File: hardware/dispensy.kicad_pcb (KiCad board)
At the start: 2 copper layers, 125 x 100 mm, 88 parts, among them SW1 BOOTSEL, SW2 RESET, U1 DBT50G-7_62-4P, U10 RP2040, U11 SS54_C22452, U12 SS54_C22452, U13 CAN_IO, U14 TJA1042T_3_1J, U15 USB-C, U16 LM2576S-5_0_TR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

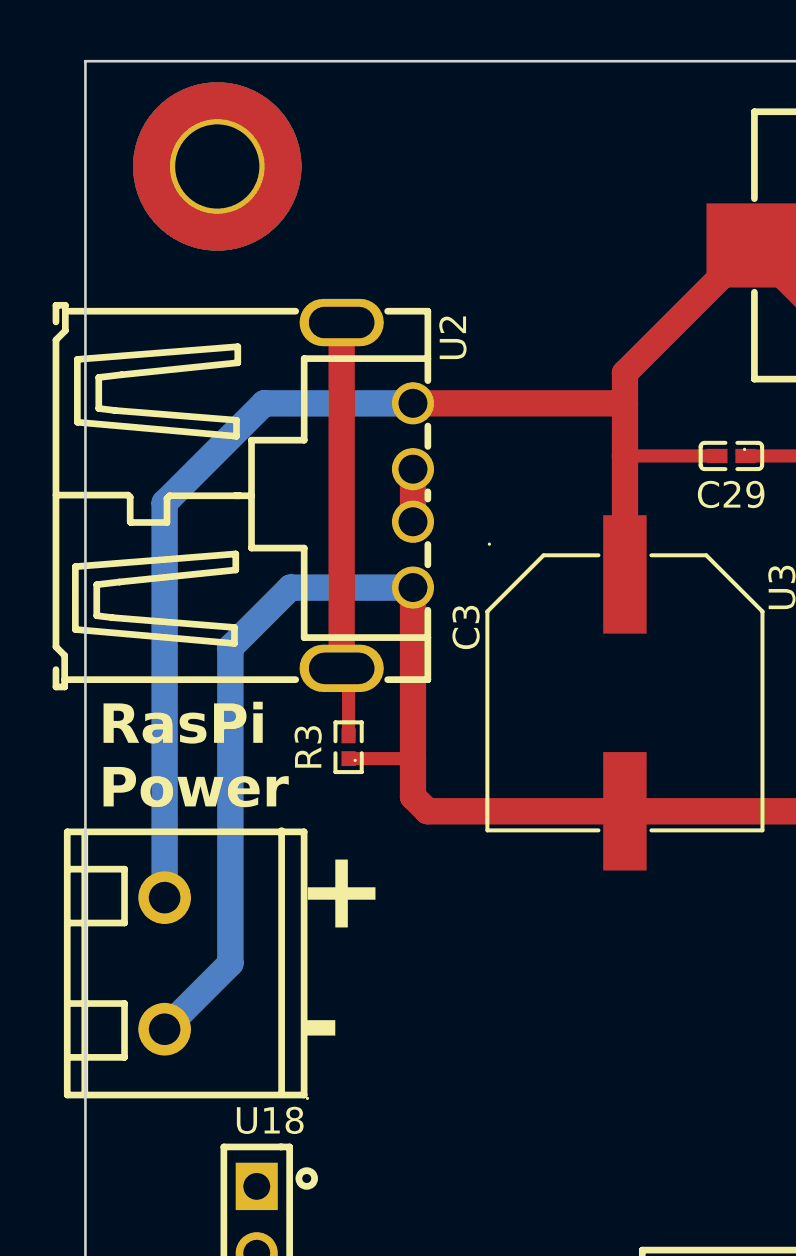
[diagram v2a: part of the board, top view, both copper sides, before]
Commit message: add resettable fuse to 5v ext output
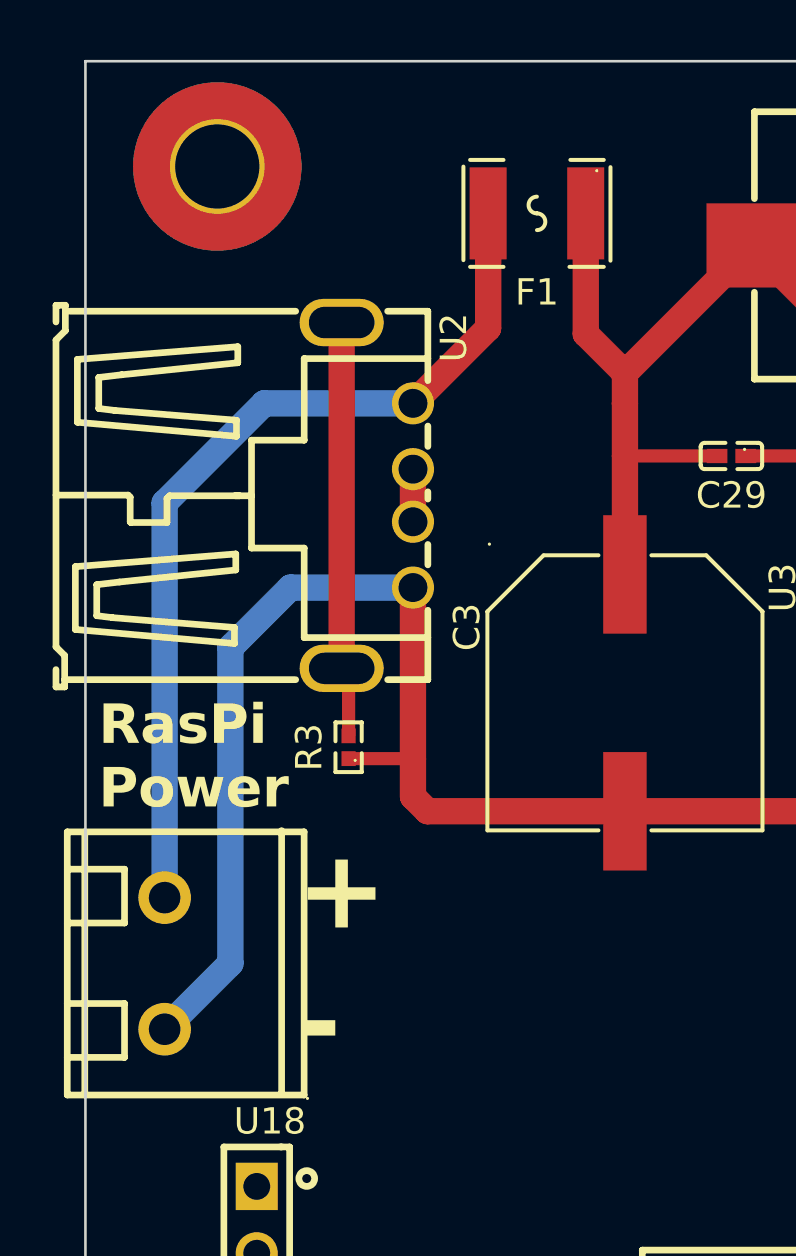
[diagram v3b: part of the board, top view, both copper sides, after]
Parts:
- added F1: ASMD1812-350-16V, jlc_footprints:F1812, F.Cu at (110.6, 53.5)
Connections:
- U18 pad 2: /EXT_PSU/Vout -> Net-(U2-VCC)
- U2 pad 1: /EXT_PSU/Vout -> Net-(U2-VCC)
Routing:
- net Net-(U2-VCC): track 0.00 -> 34.4 mm
- net /EXT_PSU/Vout: track 62.5 -> 35.1 mm
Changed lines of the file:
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@@
   (net 85 "unconnected-(U15-TX2--PadB3)")
   (net 86 "unconnected-(U15-TX2+-PadB2)")
+  (net 87 "Net-(U2-VCC)")
   (footprint "jlc_footprints:HDR-TH_3P-P2.54-V-F" (layer "F.Cu")
     (at 135.5 131.552545 180)
@@
     )
   )
+  (footprint "jlc_footprints:F1812" (layer "F.Cu")
+    (at 110.646558 53.5 180)
+    (descr "F1812 footprint")
+    (tags "F1812 footprint C2982285")
+    (property "LCSC" "C2982285")
+    (property "Sheetfile" "dispensy.kicad_sch")
+    (property "Sheetname" "")
+    (property "ki_keywords" "C2982285")
+    (attr smd)
+    (fp_text reference "F1" (at 0 -3) (layer "F.SilkS")
+        (effects (font (size 1 1) (thickness 0.15)))
+    )
+    (fp_text value "ASMD1812-350-16V" (at 0 3) (layer "F.Fab")
+        (effects (font (size 1 1) (thickness 0.15)))
+    )
+    (fp_line (start -2.794006 -1.797765) (end -2.794006 1.758242)
+      (stroke (width 0.151994) (type solid)) (layer "F.SilkS"))
+    (fp_line (start -2.540005 -2.032004) (end -1.23495 -2.032004)
+      (stroke (width 0.1524) (type solid)) (layer "F.SilkS"))
+    (fp_line (start -1.270003 2.032004) (end -2.540005 2.032004)
+      (stroke (width 0.1524) (type solid)) (layer "F.SilkS"))
+    (fp_line (start 1.270003 2.032004) (end 2.540005 2.032004)
+      (stroke (width 0.1524) (type solid)) (layer "F.SilkS"))
+    (fp_line (start 2.540005 -2.032004) (end 1.270003 -2.032004)
+      (stroke (width 0.1524) (type solid)) (layer "F.SilkS"))
+    (fp_line (start 2.794006 -1.778004) (end 2.794006 1.778004)
+      (stroke (width 0.151994) (type solid)) (layer "F.SilkS"))
+    (fp_arc (start 0 0) (mid -0.317501 -0.317501) (end 0 -0.635002)
+      (stroke (width 0.151994) (type solid)) (layer "F.SilkS"))
+    (fp_arc (start 0 0) (mid 0.317501 0.317501) (end 0 0.635002)
+      (stroke (width 0.151994) (type solid)) (layer "F.SilkS"))
+    (fp_circle (center -2.275083 1.620015) (end -2.24511 1.620015)
+      (stroke (width 0.059995) (type solid)) (fill none) (layer "F.SilkS"))
+    (pad "1" smd rect (at -1.853442 0 180) (size 1.40668 3.499213) (layers "F.Cu" "F.Paste" "F.Mask")
+      (net 4 "/EXT_PSU/Vout") (pinfunction "1") (pintype "unspecified"))
+    (pad "2" smd rect (at 1.853442 0 180) (size 1.40668 3.499213) (layers "F.Cu" "F.Paste" "F.Mask")
+      (net 87 "Net-(U2-VCC)") (pinfunction "2") (pintype "unspecified"))
+    (model "jlc_lib/jlc_footprints/packages3d/F1812.step"
+      (offset (xyz 0 0 0))
+      (scale (xyz 1 1 1))
+      (rotate (xyz 0 0 0))
+    )
+  )
   (footprint "jlc_footprints:C0402" (layer "F.Cu")
     (at 125 114.25 -90)
@@
     )
     (fp_line (start -5.000127 -3.7) (end -5.000127 5.300025)
-      (stroke (width 0.254001) (type solid)) (layer "F.SilkS"))
+      (stroke (width 0.254) (type solid)) (layer "F.SilkS"))
     (fp_line (start -5.000127 -3.7) (end 4.999873 -3.7)
-      (stroke (width 0.254001) (type solid)) (layer "F.SilkS"))
+      (stroke (width 0.254) (type solid)) (layer "F.SilkS"))
     (fp_line (start -5.000127 -3.033985) (end 4.999873 -3.033985)
-      (stroke (width 0.254001) (type solid)) (layer "F.SilkS"))
+      (stroke (width 0.254) (type solid)) (layer "F.SilkS"))
     (fp_line (start -5.000127 5.300025) (end 4.999873 5.300025)
-      (stroke (width 0.254001) (type solid)) (layer "F.SilkS"))
+      (stroke (width 0.254) (type solid)) (layer "F.SilkS"))
     (fp_line (start -4.952985 4.445034) (end 5.047015 4.445034)
-      (stroke (width 0.254001) (type solid)) (layer "F.SilkS"))
+      (stroke (width 0.254) (type solid)) (layer "F.SilkS"))
     (fp_line (start -3.569469 -3.7) (end -3.569469 -1.524003)
-      (stroke (width 0.254001) (type solid)) (layer "F.SilkS"))
+      (stroke (width 0.254) (type solid)) (layer "F.SilkS"))
     (fp_line (start -3.569469 -1.524003) (end -1.524003 -1.524003)
-      (stroke (width 0.254001) (type solid)) (layer "F.SilkS"))
+      (stroke (width 0.254) (type solid)) (layer "F.SilkS"))
     (fp_line (start -1.524003 -1.524003) (end -1.524003 -3.7)
-      (stroke (width 0.254001) (type solid)) (layer "F.SilkS"))
+      (stroke (width 0.254) (type solid)) (layer "F.SilkS"))
     (fp_line (start 1.535941 -3.7) (end 1.535941 -1.524003)
-      (stroke (width 0.254001) (type solid)) (layer "F.SilkS"))
+      (stroke (width 0.254) (type solid)) (layer "F.SilkS"))
     (fp_line (start 1.535941 -1.524003) (end 3.581407 -1.524003)
-      (stroke (width 0.254001) (type solid)) (layer "F.SilkS"))
+      (stroke (width 0.254) (type solid)) (layer "F.SilkS"))
     (fp_line (start 3.581407 -1.524003) (end 3.581407 -3.7)
-      (stroke (width 0.254001) (type solid)) (layer "F.SilkS"))
+      (stroke (width 0.254) (type solid)) (layer "F.SilkS"))
     (fp_line (start 4.999873 -3.7) (end 4.999873 5.300025)
-      (stroke (width 0.254001) (type solid)) (layer "F.SilkS"))
+      (stroke (width 0.254) (type solid)) (layer "F.SilkS"))
     (fp_circle (center -5.127127 5.426975) (end -5.097155 5.426975)
       (stroke (width 0.059995) (type solid)) (fill none) (layer "F.SilkS"))
@@
       (net 1 "GND") (pinfunction "1") (pintype "unspecified"))
     (pad "2" thru_hole circle (at 2.5 0 90) (size 2 2) (drill 1.2) (layers "*.Cu" "*.Mask")
-      (net 4 "/EXT_PSU/Vout") (pinfunction "2") (pintype "unspecified"))
+      (net 87 "Net-(U2-VCC)") (pinfunction "2") (pintype "unspecified"))
     (model "jlc_lib/jlc_footprints/packages3d/CONN-TH_XY300V-A-5.0-2P.step"
       (offset (xyz 0.2120645968 -0.799998388 6.250050906))
@@
       (stroke (width 0.4) (type solid)) (fill none) (layer "F.Fab"))
     (pad "1" thru_hole circle (at -3.499873 -1.354966 270) (size 1.6 1.6) (drill 1.100025) (layers "*.Cu" "*.Mask")
-      (net 4 "/EXT_PSU/Vout") (pinfunction "VCC") (pintype "unspecified"))
+      (net 87 "Net-(U2-VCC)") (pinfunction "VCC") (pintype "unspecified"))
     (pad "2" thru_hole circle (at -1 -1.354966 270) (size 1.6 1.6) (drill 1.100025) (layers "*.Cu" "*.Mask")
       (net 63 "Net-(U2-D+)") (pinfunction "D-") (pintype "unspecified"))
@@
   (segment (start 113.990456 62.717646) (end 113.990456 60.717646) (width 1) (layer "F.Cu") (net 4))
   (segment (start 124.290431 62.85087) (end 124.290431 60.167735) (width 1) (layer "F.Cu") (net 4))
-  (segment (start 105.936735 60.717773) (end 113.990329 60.717773) (width 1) (layer "F.Cu") (net 4))
+  (segment (start 112.5 58.077076) (end 113.990456 59.567532) (width 1) (layer "F.Cu") (net 4))
+  (segment (start 112.5 53.5) (end 112.5 58.077076) (width 1) (layer "F.Cu") (net 4))
   (segment (start 124.290431 60.167735) (end 118.840342 54.717646) (width 1) (layer "F.Cu") (net 4))
   (segment (start 113.990456 59.567532) (end 118.840342 54.717646) (width 1) (layer "F.Cu") (net 4))
@@
   (segment (start 113.990456 67.217773) (end 113.990456 62.717646) (width 1) (layer "F.Cu") (net 4))
   (segment (start 117.490456 62.717646) (end 113.990456 62.717646) (width 0.5) (layer "F.Cu") (net 4))
-  (segment (start 96.5 79.5) (end 96.5 64.5) (width 1) (layer "B.Cu") (net 4))
-  (segment (start 96.5 64.5) (end 100.282227 60.717773) (width 1) (layer "B.Cu") (net 4))
-  (segment (start 100.282227 60.717773) (end 105.936735 60.717773) (width 1) (layer "B.Cu") (net 4))
   (segment (start 191.754966 80.907765) (end 194.254966 80.907765) (width 0.5) (layer "F.Cu") (net 5))
   (segment (start 191.484963 89.177768) (end 194.984963 89.177768) (width 0.5) (layer "F.Cu") (net 5))
@@
   (segment (start 157.5 131.552545) (end 156 130.052545) (width 0.2) (layer "B.Cu") (net 76))
   (segment (start 156 130.052545) (end 155 130.052545) (width 0.2) (layer "B.Cu") (net 76))
+  (segment (start 108.793116 57.861392) (end 105.936735 60.717773) (width 1) (layer "F.Cu") (net 87))
+  (segment (start 108.793116 53.5) (end 108.793116 57.861392) (width 1) (layer "F.Cu") (net 87))
+  (segment (start 96.5 79.5) (end 96.5 64.5) (width 1) (layer "B.Cu") (net 87))
+  (segment (start 96.5 64.5) (end 100.282227 60.717773) (width 1) (layer "B.Cu") (net 87))
+  (segment (start 100.282227 60.717773) (end 105.936735 60.717773) (width 1) (layer "B.Cu") (net 87))
 )

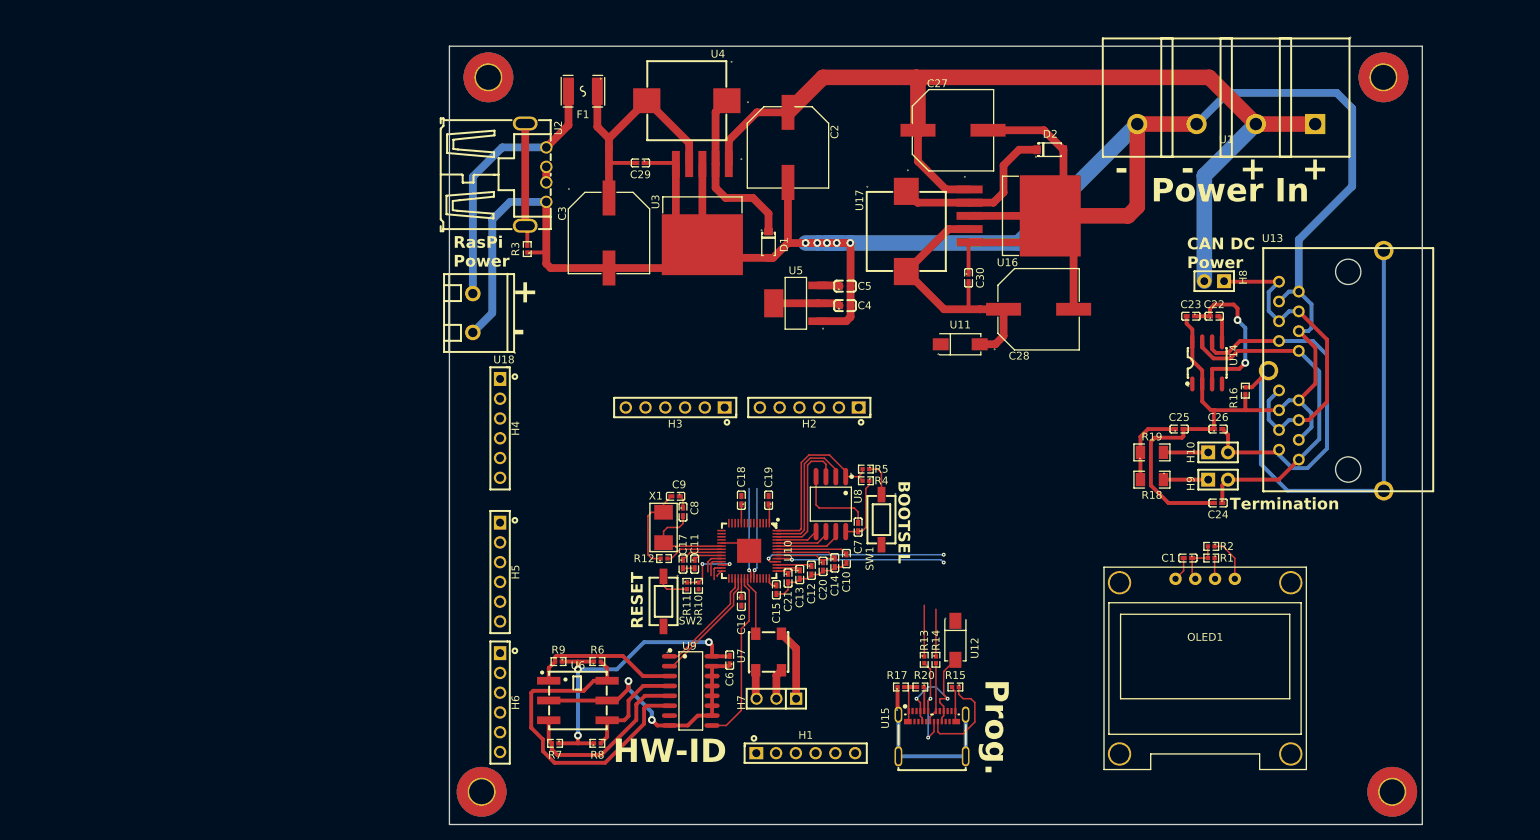
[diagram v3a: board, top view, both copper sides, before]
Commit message: fuse for main 5v. parts moved and made dimensions smaller.
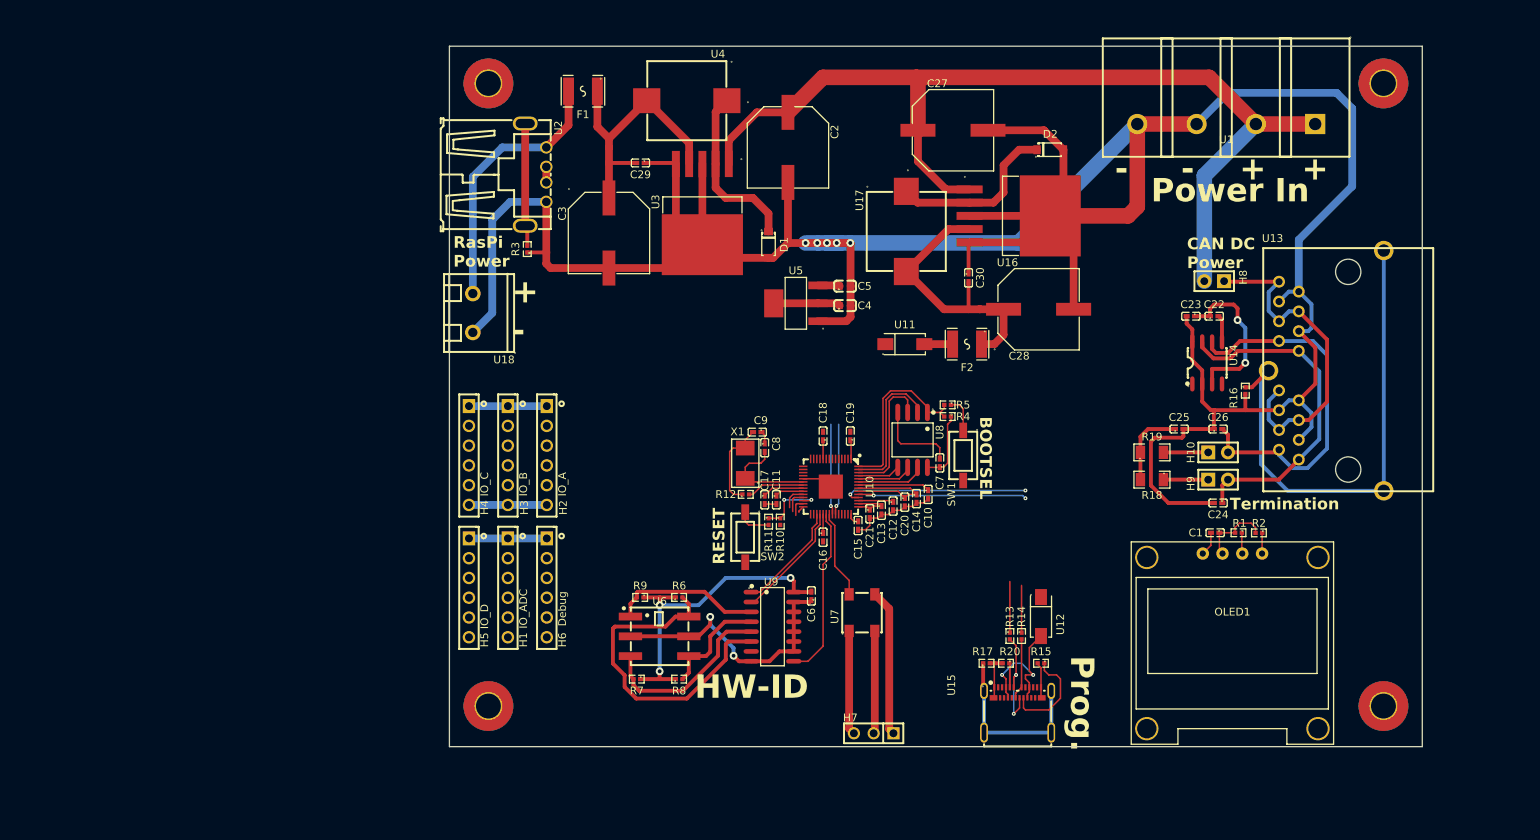
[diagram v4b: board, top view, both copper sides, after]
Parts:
- added F2: ASMD1812-350-16V, jlc_footprints:F1812, F.Cu at (160.0, 86.0)
- U11: value SS54_C22452 -> SS54
- U5: value AMS1117-3_3_C347222 -> AMS1117-3_3
- moved H1 43.8 mm to (101.0, 117.3), turned to -90 degrees
- moved H2 34.3 mm to (106.0, 100.3), turned to -90 degrees
- moved H3 22.4 mm to (101.0, 100.3), turned to -90 degrees
- moved H6 15.9 mm to (106.0, 117.3)
- moved U9 13.4 mm to (135.0, 122.3)
- moved C10 13.4 mm to (155.0, 105.3)
- moved C11 13.4 mm to (135.5, 106.0)
- moved C12 13.4 mm to (150.5, 106.8)
- moved C13 13.4 mm to (149.0, 107.3)
- moved C14 13.4 mm to (153.5, 105.8)
- moved C15 13.4 mm to (146.0, 109.3)
- moved C16 13.4 mm to (141.5, 110.8)
- moved C17 13.4 mm to (134.0, 106.0)
- moved C18 13.4 mm to (141.5, 97.8)
- moved C19 13.4 mm to (145.0, 97.8)
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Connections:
- U11 pad 1: /PI/PI_PSU/Vout -> Net-(U11-A)
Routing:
- net +3.3V: track 105.5 -> 128.5 mm
- net GND: track 479.8 -> 499.6 mm
- net +5V: track 27.3 -> 37.0 mm
- net Net-(U7-DO): track 3.92 -> 13.2 mm
- net /PI/LED_Din: track 7.53 -> 11.4 mm
- net Net-(U11-A): track 0.00 -> 3.64 mm
- net /PI/I2C_SDA: track 5.87 -> 2.67 mm
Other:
- board size 125 x 100 mm -> 125 x 90 mm
